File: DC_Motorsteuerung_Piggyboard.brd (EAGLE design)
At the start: 40 x 100 mm, 16 parts, among them X1 PFVERB10

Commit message: Piggyboard finished !!
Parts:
- moved H1 27.6 mm to (25.4, 46.4)
- moved X1 17.3 mm to (25.4, 64.1)
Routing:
- net N$1: track 0.00 -> 63.8 mm
- net N$11: track 0.00 -> 60.7 mm
- net N$3: track 0.00 -> 41.4 mm
- net N$12: track 0.00 -> 40.9 mm
- net N$9: track 0.00 -> 35.7 mm, vias 0 -> 1
- net N$8: track 0.00 -> 31.3 mm, vias 0 -> 1
- net N$5: track 0.00 -> 24.5 mm
- net N$7: track 0.00 -> 15.1 mm, vias 0 -> 1
- net N$6: track 0.00 -> 13.8 mm
- net N$4: track 0.00 -> 5.22 mm
- net N$2: track 0.00 -> 5.22 mm
- net N$15: track 0.00 -> 5.22 mm
- net N$14: track 0.00 -> 5.22 mm
- net N$13: track 0.00 -> 5.22 mm
- net N$10: track 0.00 -> 5.22 mm

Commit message: Piggyboard finished!!
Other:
- board size 40 x 100 mm -> 34.9 x 100 mm
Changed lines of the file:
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@@
 <board>
 <plain>
-<wire x1="0" y1="0" x2="39.985" y2="0" width="0" layer="20"/>
-<wire x1="39.985" y1="0" x2="39.985" y2="100" width="0" layer="20"/>
-<wire x1="39.985" y1="100" x2="0" y2="100" width="0" layer="20"/>
+<wire x1="0" y1="0" x2="34.905" y2="0" width="0" layer="20"/>
+<wire x1="34.905" y1="0" x2="34.905" y2="100" width="0" layer="20"/>
+<wire x1="34.905" y1="100" x2="0" y2="100" width="0" layer="20"/>
 <wire x1="0" y1="100" x2="0" y2="0" width="0" layer="20"/>
 </plain>
@@
 <polygon width="0.3048" layer="16" isolate="0.3048" orphans="yes">
 <vertex x="0" y="0"/>
-<vertex x="40.005" y="0"/>
-<vertex x="40.005" y="100.33"/>
+<vertex x="34.925" y="0"/>
+<vertex x="34.925" y="100.33"/>
 <vertex x="0" y="100.33"/>
 </polygon>

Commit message: Piggyboard updated and finished !! (RGB-LED included)
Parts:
- removed X1: PFVERB10, Connector:PFVERB10
- added R7, R8: 90R, Resistor:R_0,4W
- added SV2: (no value), con-lstb:MA06-2
- D6: value Motor Fuse -> (none); device Test:LED3MMCASE -> LED:RGBLED5MM
- R2, R5, R6: value 1,5 -> 1,5k
- R3: value 11k -> 1,5k
- R4: value 1,5 -> 160R
- moved D6 6.99 mm to (6.99, 43.8)
- moved R4 6.35 mm to (14.6, 38.7)
- moved S1 1.27 mm to (5.01, 73.7)
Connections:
- removed net N$8: S1.S1, U$2.P$3, X1.9
- new net N$16: R4.1, SV2.6
- new net N$17: D6.P$4, R7.2
- new net N$18: D6.P$1, R8.2
- new net N$19: D6.P$2, R4.2
- new net N$20: R6.1, SV2.5
- net GND: now also D6.P$3, SV2.11; no longer D6.P$2, X1.10
- net N$1: now also SV2.7; no longer X1.2
- net N$11: now also S1.S1, SV2.12, U$2.P$3; no longer R6.1, X1.6
- net N$12: now also SV2.1; no longer X1.5
- net N$15: now also R7.1, SV2.2; no longer D6.P$1, R4.2
- net N$3: now also SV2.3; no longer X1.1
- net N$5: now also R8.1, SV2.4; no longer R4.1, X1.4
- net N$6: now also SV2.8; no longer X1.3
- net N$7: now also SV2.9; no longer X1.8
- net N$9: now also SV2.10; no longer X1.7
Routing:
- net N$20: track 0.00 -> 70.9 mm
- net N$16: track 0.00 -> 39.6 mm
- net N$11: track 60.7 -> 22.0 mm
- net N$8: track 31.3 -> 0.00 mm, vias 1 -> 0
- net N$1: track 63.8 -> 85.5 mm
- net N$15: track 5.22 -> 24.3 mm
- net N$19: track 0.00 -> 15.7 mm
- net N$3: track 41.4 -> 56.3 mm
- net N$9: track 35.7 -> 25.3 mm, vias 1 -> 0
- net N$18: track 0.00 -> 8.15 mm
- net N$6: track 13.8 -> 20.8 mm
- net N$17: track 0.00 -> 6.61 mm
- net N$5: track 24.5 -> 18.8 mm
- net N$12: track 40.9 -> 41.7 mm
- net N$7: track 15.1 -> 15.7 mm, vias 1 -> 0
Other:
- board size 34.9 x 100 mm -> 35.2 x 100 mm

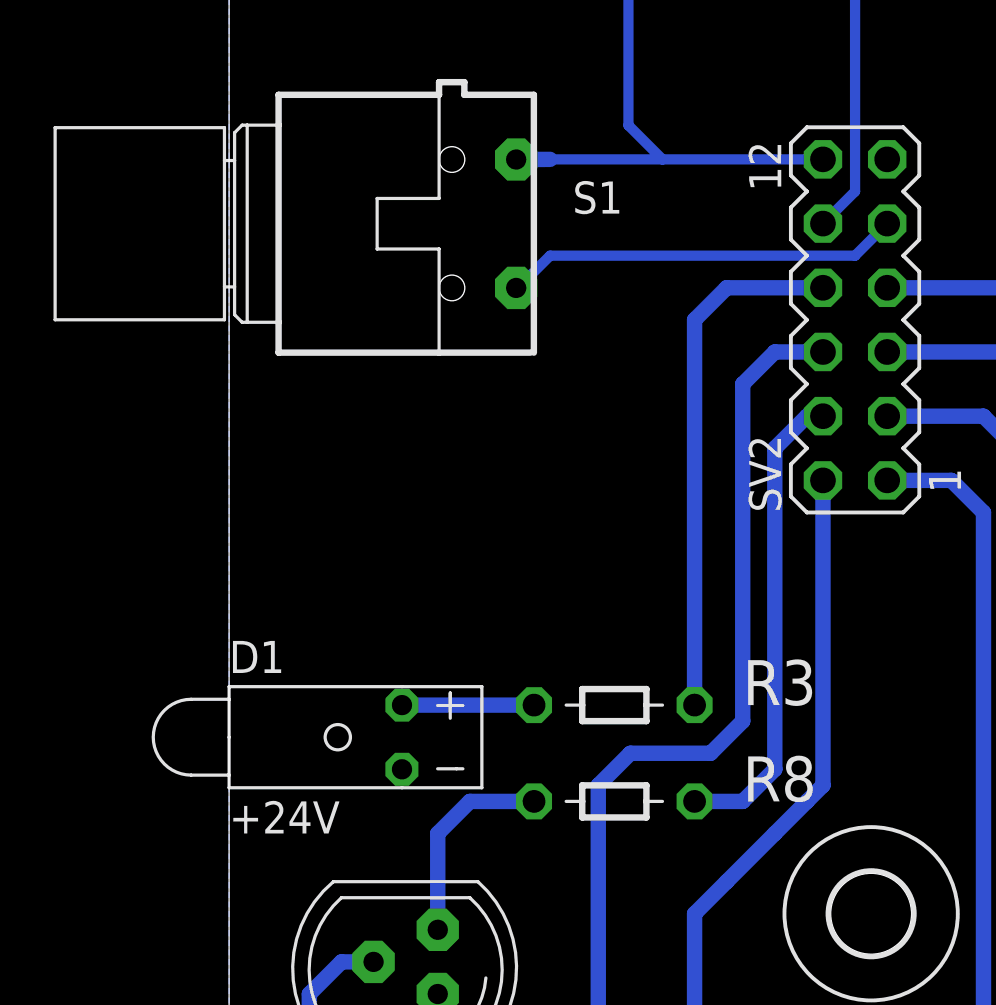
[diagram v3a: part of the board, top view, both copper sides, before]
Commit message: moved D1 for description on front plate
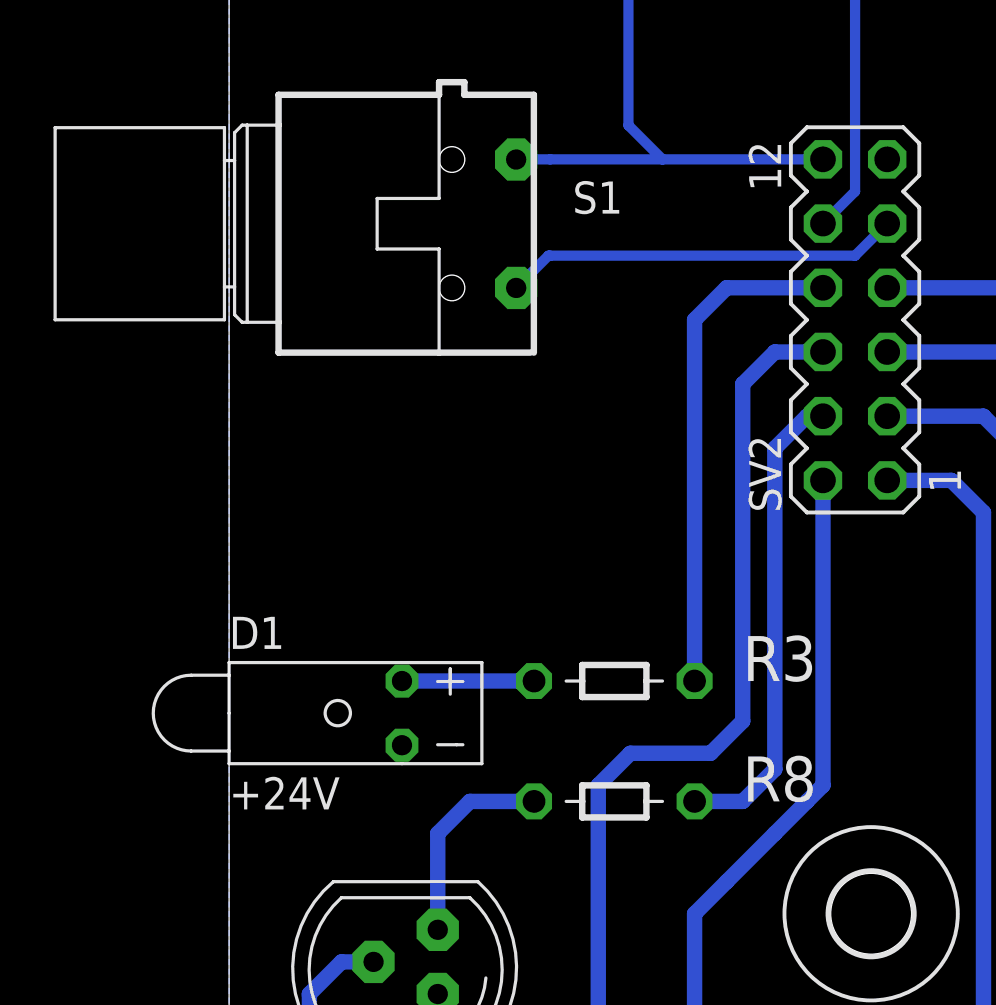
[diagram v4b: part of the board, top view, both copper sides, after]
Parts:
- moved R3 0.95 mm to (14.6, 55.6)
- moved D1 0.95 mm to (0.00, 54.3)
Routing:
- net N$6: track 20.8 -> 19.9 mm
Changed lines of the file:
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@@
 <setting verticaltext="up"/>
 </settings>
-<grid distance="0.635" unitdist="mm" unit="mm" style="dots" multiple="1" display="yes" altdistance="0.001" altunitdist="mm" altunit="mm"/>
+<grid distance="0.635" unitdist="mm" unit="mm" style="dots" multiple="1" display="yes" altdistance="0.3175" altunitdist="mm" altunit="mm"/>
 <layers>
 <layer number="1" name="Top" color="4" fill="1" visible="yes" active="yes"/>
@@
 </autorouter>
 <elements>
-<element name="D1" library="Test" package="LED3MMCASE" value="+24V" x="0" y="53.34"/>
+<element name="D1" library="Test" package="LED3MMCASE" value="+24V" x="0" y="54.2925"/>
 <element name="D2" library="Test" package="LED3MMCASE" value="Moves A" x="0" y="34.29"/>
 <element name="D3" library="Test" package="LED3MMCASE" value="Limit A" x="0" y="24.765"/>
@@
 <attribute name="VALUE" x="19.05" y="10.4775" size="1.778" layer="27" rot="R180"/>
 </element>
-<element name="R3" library="Resistor" package="R_0,4W" value="1,5k" x="14.605" y="54.61" smashed="yes" rot="R180">
-<attribute name="NAME" x="20.32" y="54.61" size="1.778" layer="25"/>
-<attribute name="VALUE" x="19.05" y="58.1025" size="1.778" layer="27" rot="R180"/>
+<element name="R3" library="Resistor" package="R_0,4W" value="1,5k" x="14.605" y="55.5625" smashed="yes" rot="R180">
+<attribute name="NAME" x="20.32" y="55.5625" size="1.778" layer="25"/>
+<attribute name="VALUE" x="19.05" y="59.055" size="1.778" layer="27" rot="R180"/>
 </element>
 <element name="R5" library="Resistor" package="R_0,4W" value="1,5k" x="14.605" y="35.56" smashed="yes" rot="R180">
@@
 <wire x1="26.035" y1="73.66" x2="24.765" y2="72.39" width="0.4064" layer="16"/>
 <wire x1="24.765" y1="72.39" x2="12.7" y2="72.39" width="0.4064" layer="16"/>
-<wire x1="12.7" y1="72.39" x2="11.43" y2="71.12" width="0.4064" layer="16"/>
-<wire x1="11.43" y1="71.12" x2="11.357" y2="71.114" width="0.4064" layer="16"/>
+<wire x1="12.7" y1="72.39" x2="12.633" y2="72.39" width="0.4064" layer="16"/>
+<wire x1="12.633" y1="72.39" x2="11.357" y2="71.114" width="0.4064" layer="16"/>
 </signal>
 <signal name="N$9">
@@
 <contactref element="R3" pad="1"/>
 <contactref element="SV2" pad="8"/>
-<wire x1="18.415" y1="54.61" x2="18.415" y2="69.85" width="0.6096" layer="16"/>
+<wire x1="18.415" y1="55.5625" x2="18.415" y2="69.85" width="0.6096" layer="16"/>
 <wire x1="18.415" y1="69.85" x2="19.685" y2="71.12" width="0.6096" layer="16"/>
 <wire x1="19.685" y1="71.12" x2="23.495" y2="71.12" width="0.6096" layer="16"/>
@@
 <contactref element="D1" pad="P$1"/>
 <contactref element="R3" pad="2"/>
-<wire x1="6.84" y1="54.61" x2="12.065" y2="54.61" width="0.6096" layer="16"/>
+<wire x1="6.84" y1="55.5625" x2="12.065" y2="55.5625" width="0.6096" layer="16"/>
 </signal>
 <signal name="N$1">
@@
 <wire x1="23.495" y1="76.2" x2="17.145" y2="76.2" width="0.4064" layer="16"/>
 <wire x1="17.145" y1="76.2" x2="12.7" y2="76.2" width="0.4064" layer="16"/>
-<wire x1="12.7" y1="76.2" x2="11.357" y2="76.194" width="0.6096" layer="16"/>
 <wire x1="15.8" y1="85.47" x2="15.8" y2="77.545" width="0.4064" layer="16"/>
 <wire x1="15.8" y1="77.545" x2="17.145" y2="76.2" width="0.4064" layer="16"/>
+<wire x1="12.7" y1="76.2" x2="11.357" y2="76.2" width="0.4064" layer="16"/>
+<wire x1="11.357" y1="76.2" x2="11.357" y2="76.194" width="0.4064" layer="16"/>
 </signal>
 </signals>
